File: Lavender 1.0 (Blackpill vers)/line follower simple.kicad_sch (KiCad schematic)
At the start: 36 parts, among them J1 XT30UPB-M, J14 Conn_01x20_MountingPin, J2 Conn_01x20_MountingPin, J3 Conn_01x02_Pin, J4 Conn_01x02_Pin, J6 Conn_01x20_MountingPin, J7 Conn_01x20_MountingPin, J9 Conn_01x20_MountingPin, SW2 SW_Push, SW3 SW_Push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

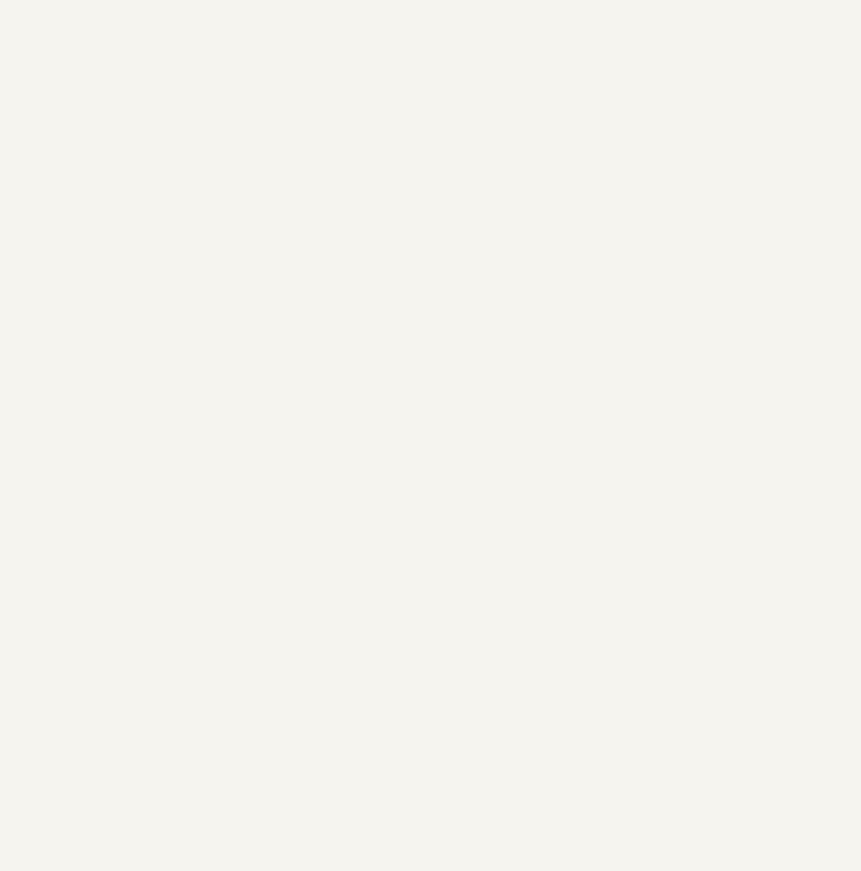
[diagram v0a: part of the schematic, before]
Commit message: Add mousebites
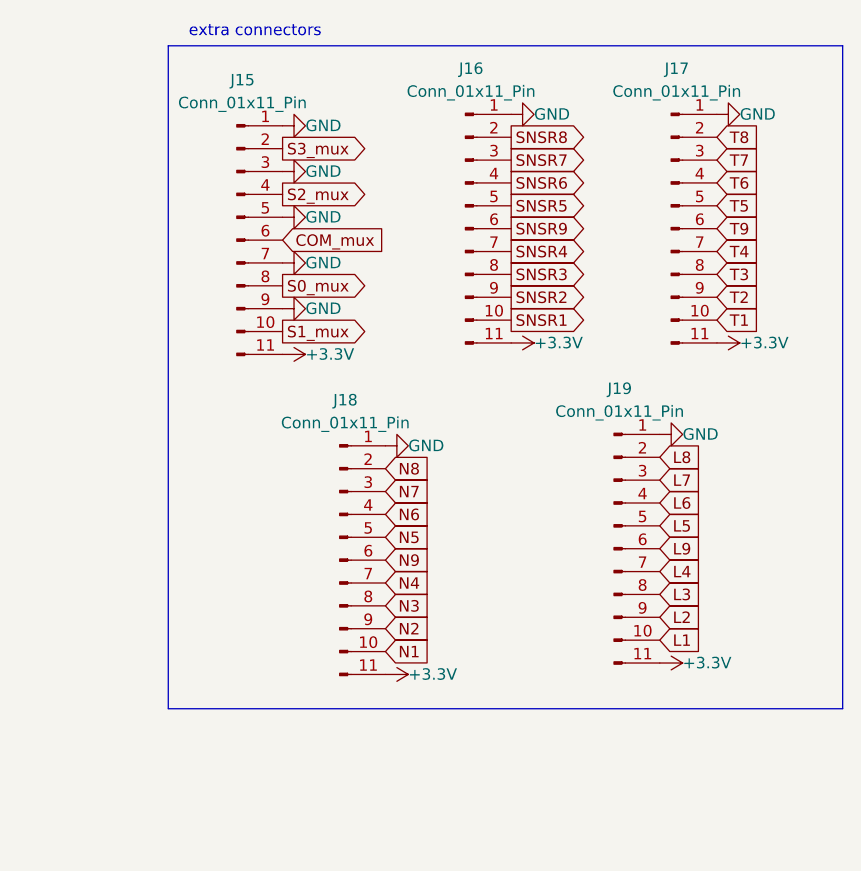
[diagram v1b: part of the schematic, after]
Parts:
- added J15, J16, J17, J18, J19: Conn_01x11_Pin, Connector_PinHeader_2.54mm:PinHeader_1x11_P2.54mm_Vertical, symbol Connector:Conn_01x11_Pin
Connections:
- net +3.3V: now also J15.11 (Pin_11), J16.11 (Pin_11), J17.11 (Pin_11), J18.11 (Pin_11), J19.11 (Pin_11)
- net COM_mux: now also J15.6 (Pin_6)
- net GND: now also J15.1 (Pin_1), J15.3 (Pin_3), J15.5 (Pin_5), J15.7 (Pin_7), J15.9 (Pin_9), J16.1 (Pin_1), J17.1 (Pin_1), J18.1 (Pin_1), J19.1 (Pin_1)
- net L1: now also J19.10 (Pin_10)
- net L2: now also J19.9 (Pin_9)
- net L3: now also J19.8 (Pin_8)
- net L4: now also J19.7 (Pin_7)
- net L5: now also J19.5 (Pin_5)
- net L6: now also J19.4 (Pin_4)
- net L7: now also J19.3 (Pin_3)
- net L8: now also J19.2 (Pin_2)
- net L9: now also J19.6 (Pin_6)
- net N1: now also J18.10 (Pin_10)
- net N2: now also J18.9 (Pin_9)
- net N3: now also J18.8 (Pin_8)
- net N4: now also J18.7 (Pin_7)
- net N5: now also J18.5 (Pin_5)
- net N6: now also J18.4 (Pin_4)
- net N7: now also J18.3 (Pin_3)
- net N8: now also J18.2 (Pin_2)
- net N9: now also J18.6 (Pin_6)
- net S0_mux: now also J15.8 (Pin_8)
- net S1_mux: now also J15.10 (Pin_10)
- net S2_mux: now also J15.4 (Pin_4)
- net S3_mux: now also J15.2 (Pin_2)
- net SNSR1: now also J16.10 (Pin_10)
- net SNSR2: now also J16.9 (Pin_9)
- net SNSR3: now also J16.8 (Pin_8)
- net SNSR4: now also J16.7 (Pin_7)
- net SNSR5: now also J16.5 (Pin_5)
- net SNSR6: now also J16.4 (Pin_4)
- net SNSR7: now also J16.3 (Pin_3)
- net SNSR8: now also J16.2 (Pin_2)
- net SNSR9: now also J16.6 (Pin_6)
- net T1: now also J17.10 (Pin_10)
- net T2: now also J17.9 (Pin_9)
- net T3: now also J17.8 (Pin_8)
- net T4: now also J17.7 (Pin_7)
- net T5: now also J17.5 (Pin_5)
- net T6: now also J17.4 (Pin_4)
- net T7: now also J17.3 (Pin_3)
- net T8: now also J17.2 (Pin_2)
- net T9: now also J17.6 (Pin_6)
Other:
- note added: "extra connectors"

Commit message: Add JST for motor
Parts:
- J3, J4: footprint Connector_PinHeader_2.54mm:PinHeader_1x02_P2.54mm_Vertical -> Connector_JST:JST_PH_B2B-PH-K_1x02_P2.00mm_Vertical
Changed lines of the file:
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@@
 			)
 		)
-		(property "Footprint" "Connector_PinHeader_2.54mm:PinHeader_1x02_P2.54mm_Vertical"
+		(property "Footprint" "Connector_JST:JST_PH_B2B-PH-K_1x02_P2.00mm_Vertical"
 			(at 96.52 27.94 0)
 			(hide yes)
@@
 			)
 		)
-		(property "Footprint" "Connector_PinHeader_2.54mm:PinHeader_1x02_P2.54mm_Vertical"
+		(property "Footprint" "Connector_JST:JST_PH_B2B-PH-K_1x02_P2.00mm_Vertical"
 			(at 96.52 36.83 0)
 			(hide yes)

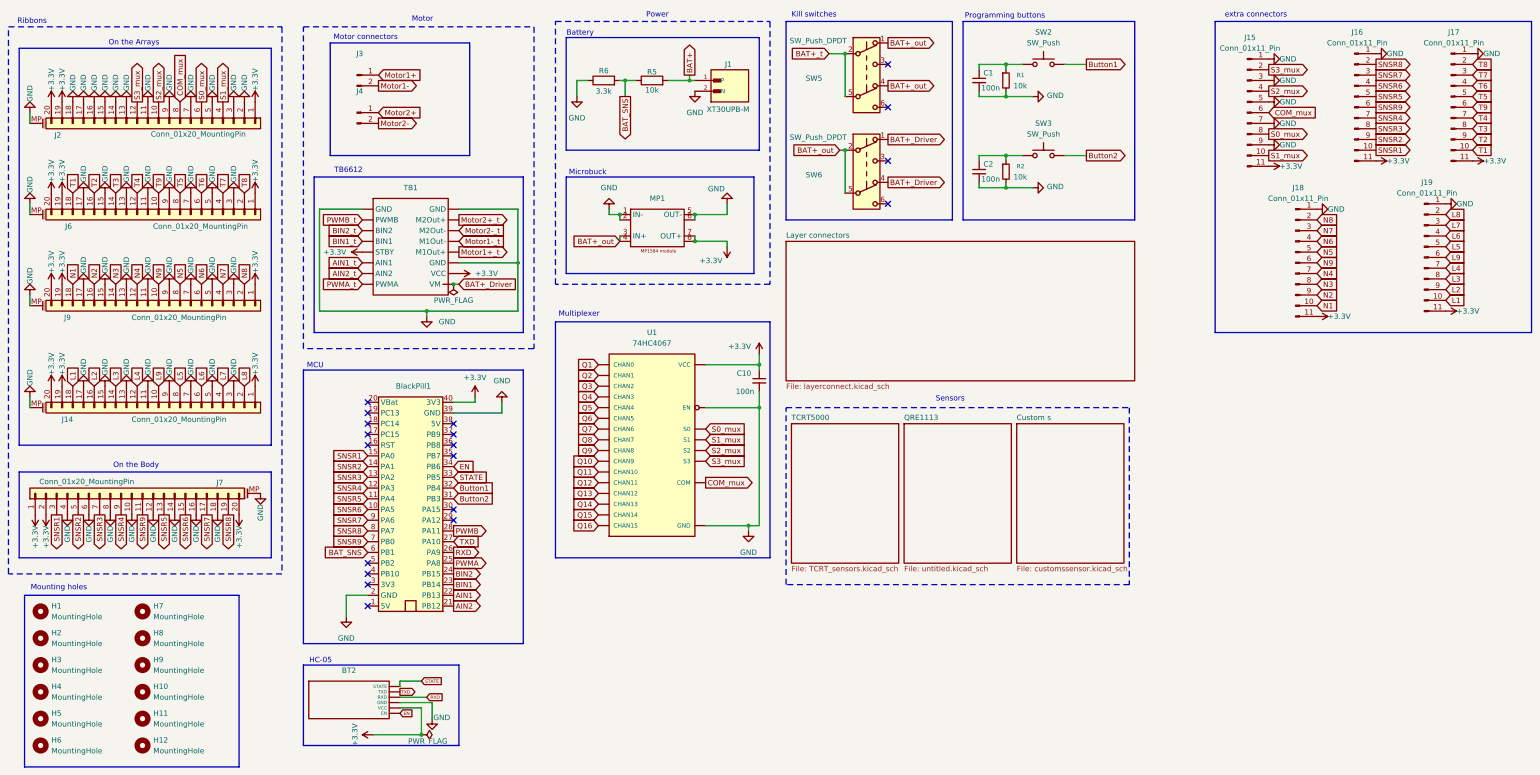
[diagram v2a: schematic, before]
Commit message: Add polyfuse
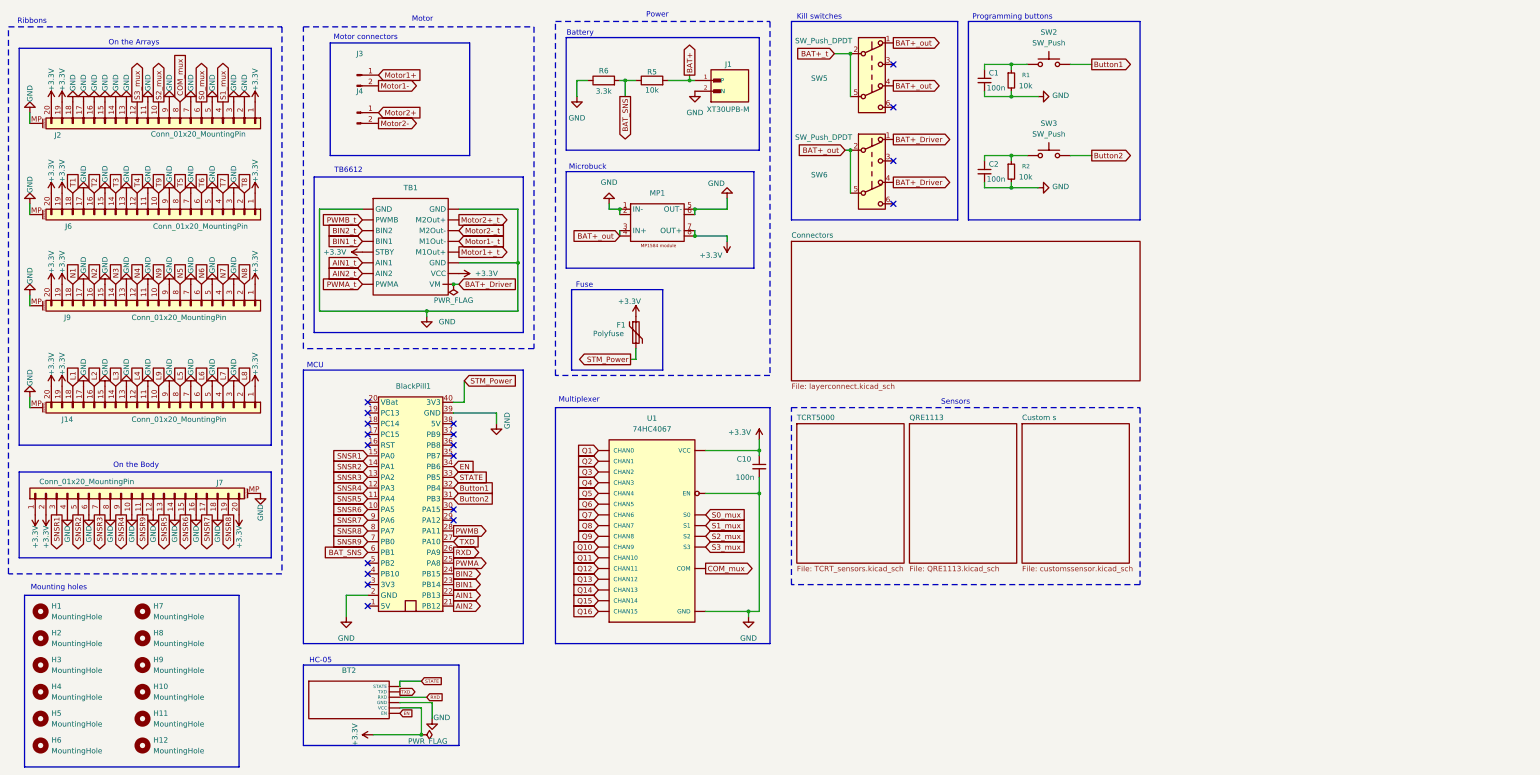
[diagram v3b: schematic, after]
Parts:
- removed J15, J16, J17, J18, J19: Conn_01x11_Pin, Connector_PinHeader_2.54mm:PinHeader_1x11_P2.54mm_Vertical, symbol Connector:Conn_01x11_Pin
- added F1: Polyfuse, Fuse:Fuse_0805_2012Metric_Pad1.15x1.40mm_HandSolder, symbol Device:Polyfuse
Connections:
- net +3.3V: now also F1.1; no longer BlackPill1.40 (3V3)
- new net STM_Power: BlackPill1.40 (3V3), F1.2
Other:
- sheet Layer connectors renamed Connectors
- sheet QRE1113: file untitled.kicad_sch -> QRE1113.kicad_sch
- note added: "Fuse"
- note removed: "extra connectors"
- moved on the sheet: C1, C10, C2, MP1, R1, R2, SW2, SW3, SW5, SW6, U1
